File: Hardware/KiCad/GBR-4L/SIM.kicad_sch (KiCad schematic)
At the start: 0 parts

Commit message: Add modem and SIM schematics
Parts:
- added C511, C521, C531, C541: 4.7uF X5R, Capacitor_SMD:C_0805_2012Metric, symbol Device:C
- added C512, C522, C532, C542: 100nF, Capacitor_SMD:C_0603_1608Metric, symbol Device:C
- added J511, J521, J531, J541: 2452808-1 nano-SIM, symbol Connector:SIM_Card_Shielded
- added R511, R521, R531, R541: 22k DNP, Resistor_SMD:R_0603_1608Metric, symbol Device:R
- added SW511, SW521, SW531, SW541: CARD_DETECT_NC, symbol Switch:SW_SPST
- added U511, U521, U531, U541: LOW-CAP SIM ESD ARRAY, Package_TO_SOT_SMD:SOT-23-6, symbol Power_Protection:ESDA6V1-5SC6
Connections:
- new net GND: C511.2, C512.2, C521.2, C522.2, C531.2, C532.2, C541.2, C542.2, J511.5 (GND), J511.SH, J521.5 (GND), J521.SH, J531.5 (GND), J531.SH, J541.5 (GND), J541.SH, SW511.2 (B), SW521.2 (B), SW531.2 (B), SW541.2 (B), U511.2 (GND), U521.2 (GND), U531.2 (GND), U541.2 (GND)
- new net M1_SIM_DETECT: SW511.1 (A), U511.6 (IO5)
- new net M1_UIM_CLK: J511.3 (CLK), U511.4 (IO3)
- new net M1_UIM_DATA: J511.7 (I/O), R511.2, U511.5 (IO4)
- new net M1_UIM_PWR: C511.1, C512.1, J511.1 (VCC), R511.1, U511.1 (IO1)
- new net M1_UIM_RESET: J511.2 (RST), U511.3 (IO2)
- new net M2_SIM_DETECT: SW521.1 (A), U521.6 (IO5)
- new net M2_UIM_CLK: J521.3 (CLK), U521.4 (IO3)
- new net M2_UIM_DATA: J521.7 (I/O), R521.2, U521.5 (IO4)
- new net M2_UIM_PWR: C521.1, C522.1, J521.1 (VCC), R521.1, U521.1 (IO1)
- new net M2_UIM_RESET: J521.2 (RST), U521.3 (IO2)
- new net M3_SIM_DETECT: SW531.1 (A), U531.6 (IO5)
- new net M3_UIM_CLK: J531.3 (CLK), U531.4 (IO3)
- new net M3_UIM_DATA: J531.7 (I/O), R531.2, U531.5 (IO4)
- new net M3_UIM_PWR: C531.1, C532.1, J531.1 (VCC), R531.1, U531.1 (IO1)
- new net M3_UIM_RESET: J531.2 (RST), U531.3 (IO2)
- new net M4_SIM_DETECT: SW541.1 (A), U541.6 (IO5)
- new net M4_UIM_CLK: J541.3 (CLK), U541.4 (IO3)
- new net M4_UIM_DATA: J541.7 (I/O), R541.2, U541.5 (IO4)
- new net M4_UIM_PWR: C541.1, C542.1, J541.1 (VCC), R541.1, U541.1 (IO1)
- new net M4_UIM_RESET: J541.2 (RST), U541.3 (IO2)
- no-connect marks 0 -> 4
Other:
- note added: "DNP pull-ups and clock termination are tuning options; populate only after signal-integrity testing."
- note added: "Detect switch: closed when card absent, open when inserted."
- note added: "ESD arrays must be low-capacitance and placed at the user-accessible socket."
- note added: "FOUR PRIMARY NANO-SIM INTERFACES"
- note added: "SIM 1"
- note added: "SIM 2"
- note added: "SIM 3"
- note added: "SIM 4"
- note added: "Sockets are placed within 100 mm of their associated EM7565. Keep CLK and DATA short and non-parallel."
- note added: "The selected socket footprint remains unassigned pending drawing and JLCPCB assembly review."
- title: (none) -> GBR-4L primary nano-SIM interfaces

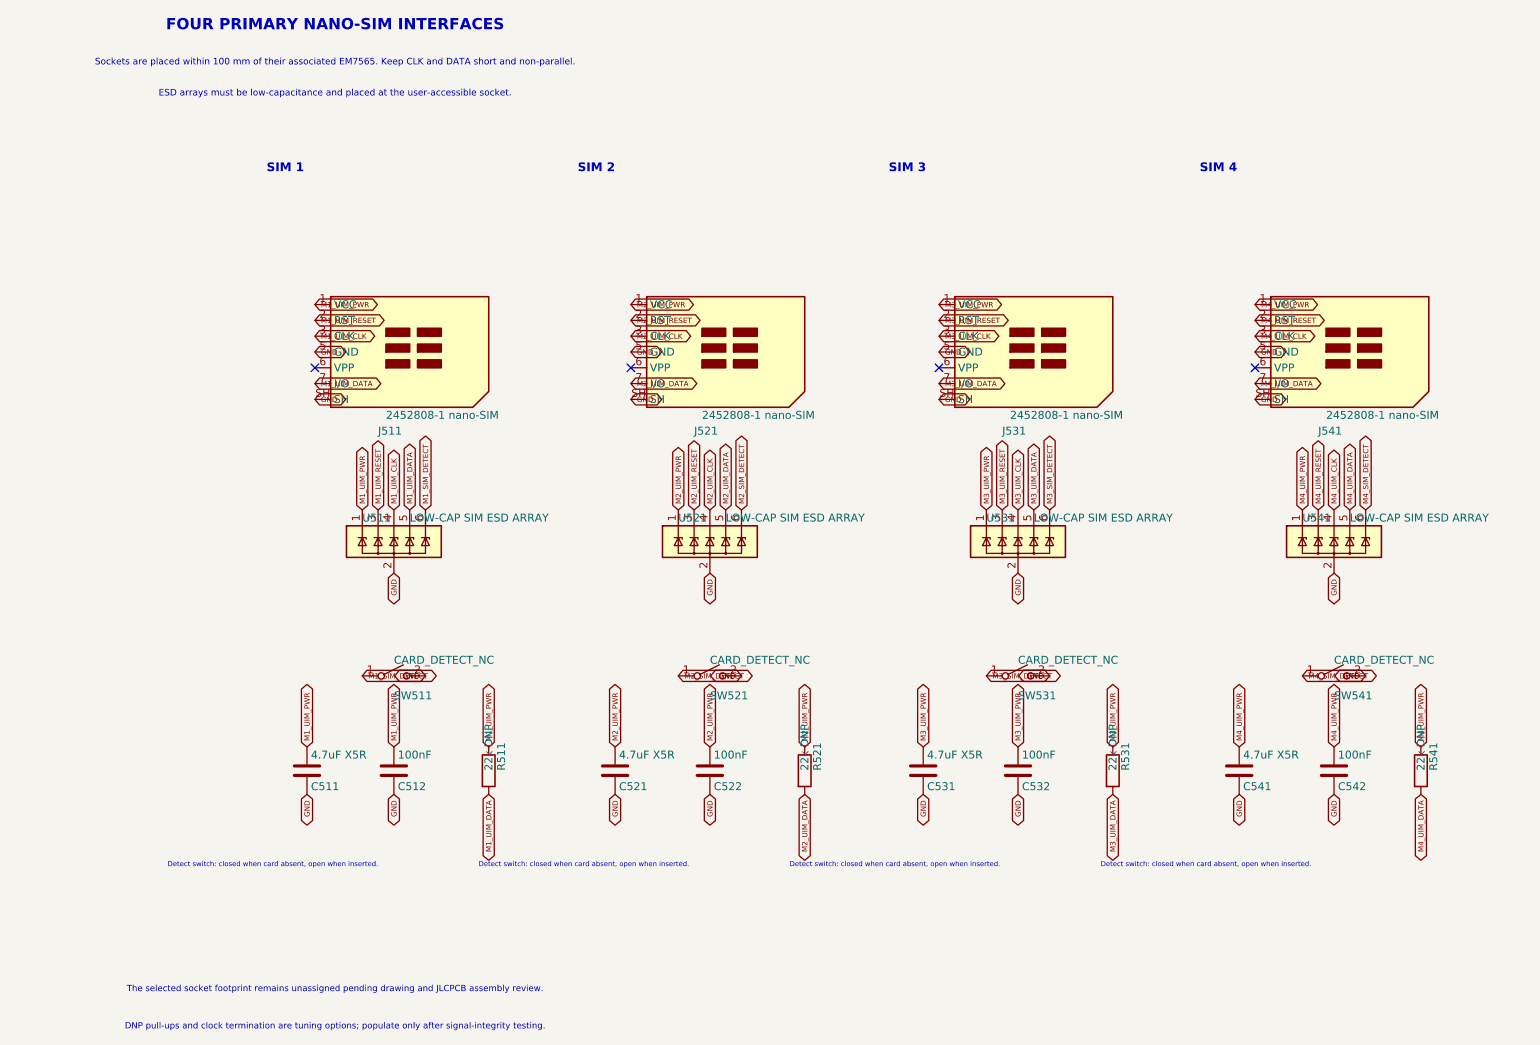
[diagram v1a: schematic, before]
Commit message: Add nano-SIM footprint and fix card detect
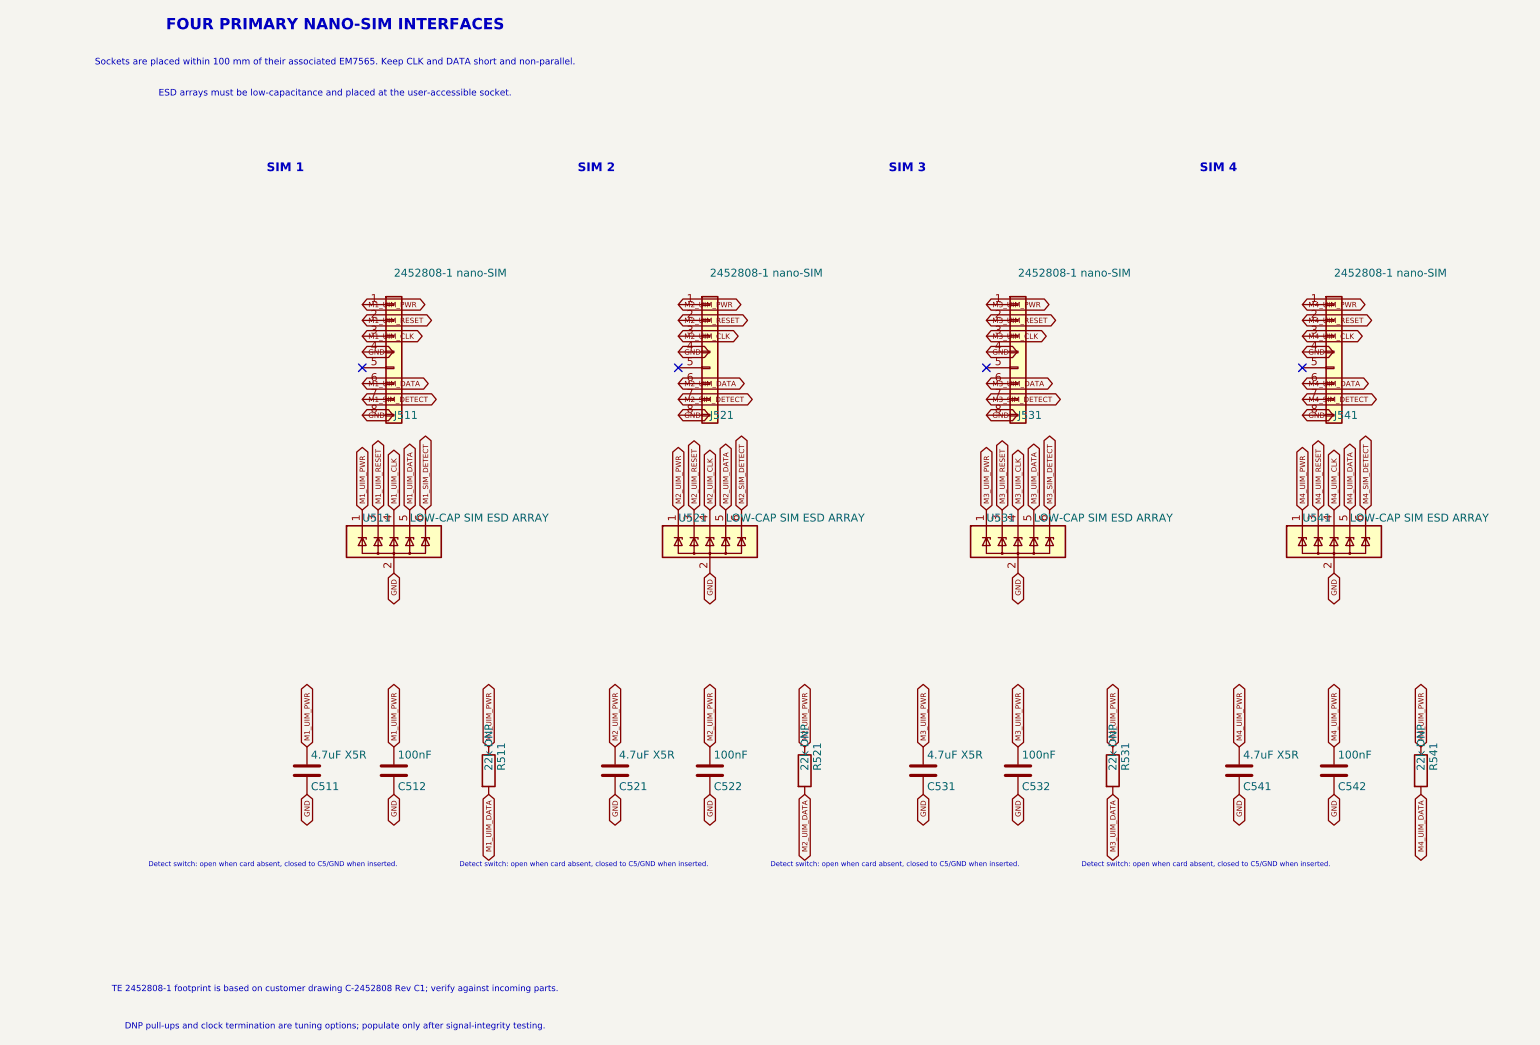
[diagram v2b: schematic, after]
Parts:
- removed J511, J521, J531, J541: 2452808-1 nano-SIM, symbol Connector:SIM_Card_Shielded
- removed SW511, SW521, SW531, SW541: CARD_DETECT_NC, symbol Switch:SW_SPST
- added J511, J521, J531, J541: 2452808-1 nano-SIM, GBR-4L:TE_2452808-1, symbol Connector_Generic:Conn_01x08
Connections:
- net GND: now also J511.4 (Pin_4), J511.8 (Pin_8), J521.4 (Pin_4), J521.8 (Pin_8), J531.4 (Pin_4), J531.8 (Pin_8), J541.4 (Pin_4), J541.8 (Pin_8)
- net M1_SIM_DETECT: now also J511.7 (Pin_7)
- net M1_UIM_CLK: now also J511.3 (Pin_3)
- net M1_UIM_DATA: now also J511.6 (Pin_6)
- net M1_UIM_PWR: now also J511.1 (Pin_1)
- net M1_UIM_RESET: now also J511.2 (Pin_2)
- net M2_SIM_DETECT: now also J521.7 (Pin_7)
- net M2_UIM_CLK: now also J521.3 (Pin_3)
- net M2_UIM_DATA: now also J521.6 (Pin_6)
- net M2_UIM_PWR: now also J521.1 (Pin_1)
- net M2_UIM_RESET: now also J521.2 (Pin_2)
- net M3_SIM_DETECT: now also J531.7 (Pin_7)
- net M3_UIM_CLK: now also J531.3 (Pin_3)
- net M3_UIM_DATA: now also J531.6 (Pin_6)
- net M3_UIM_PWR: now also J531.1 (Pin_1)
- net M3_UIM_RESET: now also J531.2 (Pin_2)
- net M4_SIM_DETECT: now also J541.7 (Pin_7)
- net M4_UIM_CLK: now also J541.3 (Pin_3)
- net M4_UIM_DATA: now also J541.6 (Pin_6)
- net M4_UIM_PWR: now also J541.1 (Pin_1)
- net M4_UIM_RESET: now also J541.2 (Pin_2)
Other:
- note added: "Detect switch: open when card absent, closed to C5/GND when inserted."
- note added: "TE 2452808-1 footprint is based on customer drawing C-2452808 Rev C1; verify against incoming parts."
- note removed: "Detect switch: closed when card absent, open when inserted."
- note removed: "The selected socket footprint remains unassigned pending drawing and JLCPCB assembly review."

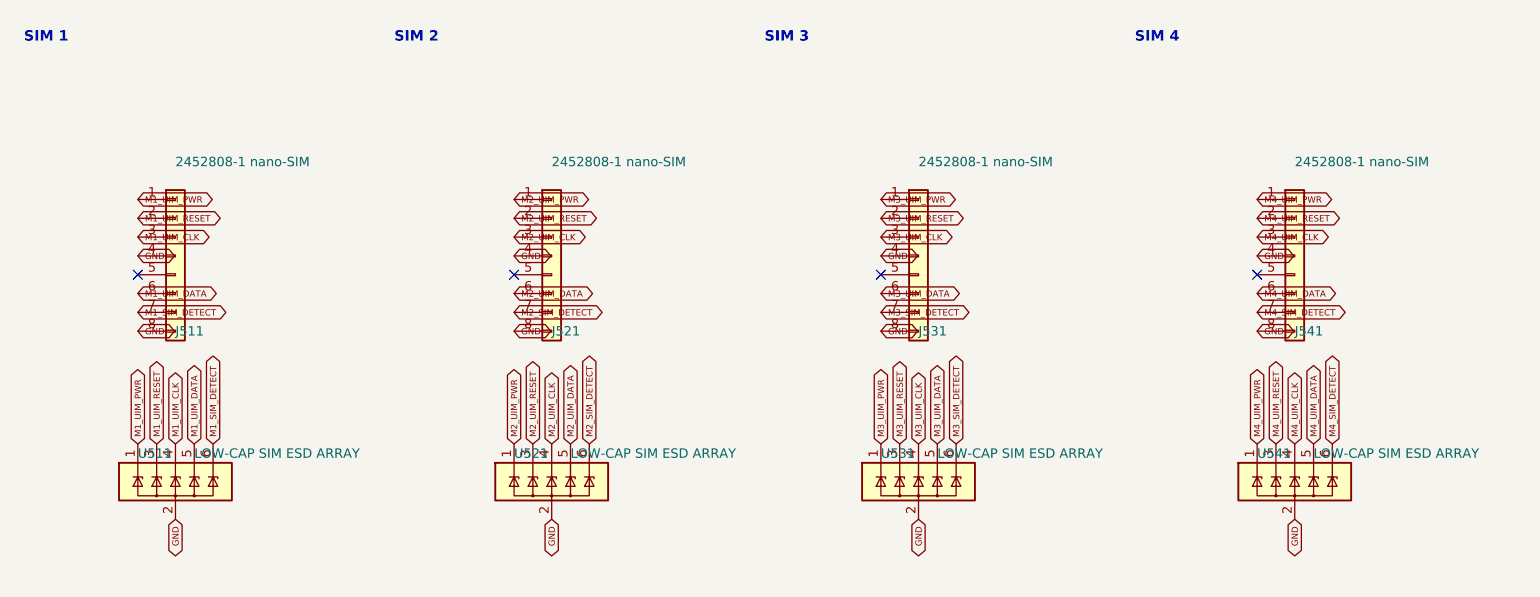
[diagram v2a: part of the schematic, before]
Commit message: Add connector footprints and initial PCB packing
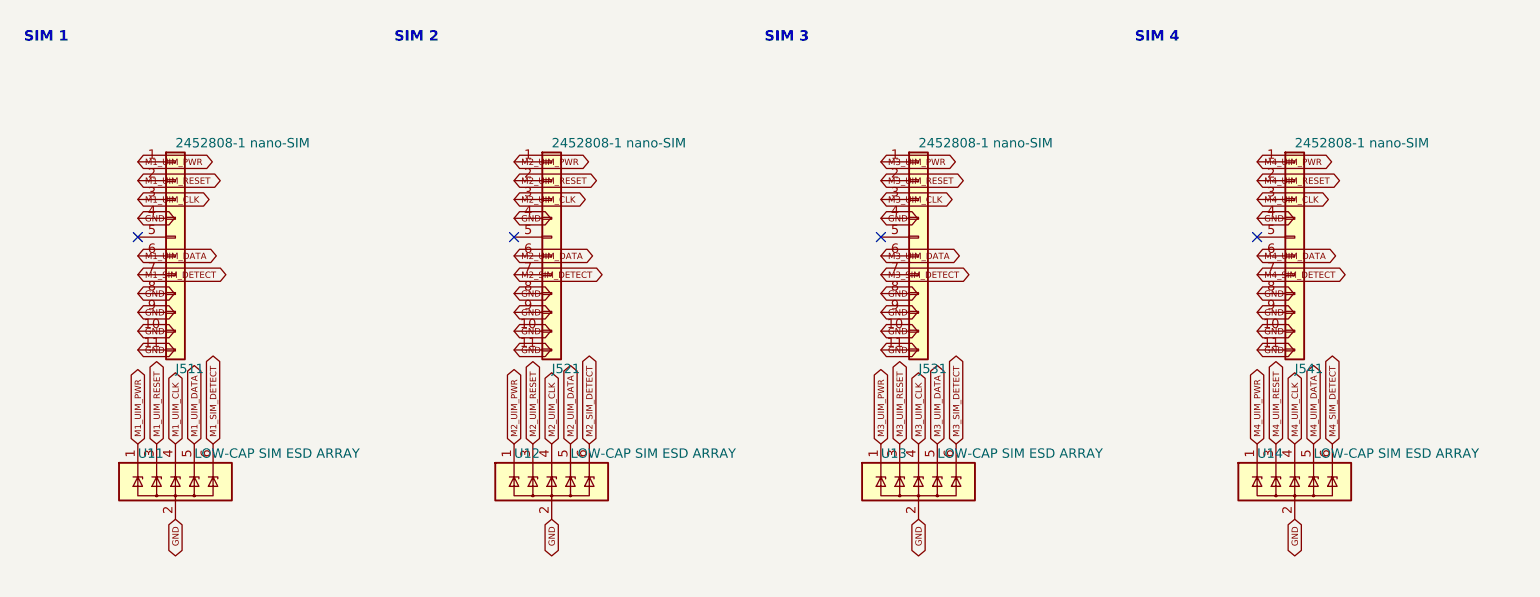
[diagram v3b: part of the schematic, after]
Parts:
- removed J511, J521, J531, J541: 2452808-1 nano-SIM, GBR-4L:TE_2452808-1, symbol Connector_Generic:Conn_01x08
- removed U511, U521, U531, U541: LOW-CAP SIM ESD ARRAY, Package_TO_SOT_SMD:SOT-23-6, symbol Power_Protection:ESDA6V1-5SC6
- added J511, J521, J531, J541: 2452808-1 nano-SIM, GBR-4L:TE_2452808-1, symbol Connector_Generic:Conn_01x11
- added U11, U12, U13, U14: LOW-CAP SIM ESD ARRAY, Package_TO_SOT_SMD:SOT-23-6, symbol Power_Protection:ESDA6V1-5SC6
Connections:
- net GND: now also J511.10 (Pin_10), J511.11 (Pin_11), J511.4 (Pin_4), J511.8 (Pin_8), J511.9 (Pin_9), J521.10 (Pin_10), J521.11 (Pin_11), J521.4 (Pin_4), J521.8 (Pin_8), J521.9 (Pin_9), J531.10 (Pin_10), J531.11 (Pin_11), J531.4 (Pin_4), J531.8 (Pin_8), J531.9 (Pin_9), J541.10 (Pin_10), J541.11 (Pin_11), J541.4 (Pin_4), J541.8 (Pin_8), J541.9 (Pin_9), U11.2 (GND), U12.2 (GND), U13.2 (GND), U14.2 (GND)
- net M1_SIM_DETECT: now also J511.7 (Pin_7), U11.6 (IO5)
- net M1_UIM_CLK: now also J511.3 (Pin_3), U11.4 (IO3)
- net M1_UIM_DATA: now also J511.6 (Pin_6), U11.5 (IO4)
- net M1_UIM_PWR: now also J511.1 (Pin_1), U11.1 (IO1)
- net M1_UIM_RESET: now also J511.2 (Pin_2), U11.3 (IO2)
- net M2_SIM_DETECT: now also J521.7 (Pin_7), U12.6 (IO5)
- net M2_UIM_CLK: now also J521.3 (Pin_3), U12.4 (IO3)
- net M2_UIM_DATA: now also J521.6 (Pin_6), U12.5 (IO4)
- net M2_UIM_PWR: now also J521.1 (Pin_1), U12.1 (IO1)
- net M2_UIM_RESET: now also J521.2 (Pin_2), U12.3 (IO2)
- net M3_SIM_DETECT: now also J531.7 (Pin_7), U13.6 (IO5)
- net M3_UIM_CLK: now also J531.3 (Pin_3), U13.4 (IO3)
- net M3_UIM_DATA: now also J531.6 (Pin_6), U13.5 (IO4)
- net M3_UIM_PWR: now also J531.1 (Pin_1), U13.1 (IO1)
- net M3_UIM_RESET: now also J531.2 (Pin_2), U13.3 (IO2)
- net M4_SIM_DETECT: now also J541.7 (Pin_7), U14.6 (IO5)
- net M4_UIM_CLK: now also J541.3 (Pin_3), U14.4 (IO3)
- net M4_UIM_DATA: now also J541.6 (Pin_6), U14.5 (IO4)
- net M4_UIM_PWR: now also J541.1 (Pin_1), U14.1 (IO1)
- net M4_UIM_RESET: now also J541.2 (Pin_2), U14.3 (IO2)
